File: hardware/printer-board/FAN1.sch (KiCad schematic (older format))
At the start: 8 parts, among them J39 TO FAN1, Q1 D882

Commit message: update,
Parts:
- J39: footprint footprint-lib:s2b-ph-kl,fan_output -> footprint-lib:b2b-ph-kl,fan_pwm_out
- Q1: footprint Package_TO_SOT_SMD:SOT-89-3 -> footprint-lib:SOT-89-3,thermal_vias
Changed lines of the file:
@@
 $Descr A4 11693 8268
 encoding utf-8
-Sheet 1 29
+Sheet 23 29
 Title ""
 Date ""
@@
 AR Path="/5CC2401E/5CC242A1/5CC8A035" Ref="J?"  Part="1"
 AR Path="/5CC2401E/5CC24321/5CC8A035" Ref="J39"  Part="1"
-AR Path="/5CC8A035" Ref="J1"  Part="1"
-F 0 "J39" H 4300 2550 50  0000 C CNN
-F 1 "TO FAN1" H 4300 2650 50  0000 C CNN
-F 2 "footprint-lib:s2b-ph-kl,fan_output" H 4350 2900 50  0001 C CNN
+AR Path="/5CC8A035" Ref="J39"  Part="1"
+F 0 "J39" H 4350 3000 50  0000 C CNN
+F 1 "TO FAN1" H 4350 2700 50  0000 C CNN
+F 2 "footprint-lib:b2b-ph-kl,fan_pwm_out" H 4350 2900 50  0001 C CNN
 F 3 "~" H 4350 2900 50  0001 C CNN
 	1    4350 2900
@@
 AR Path="/5CC2401E/5CC242A1/5CC8A041" Ref="C?"  Part="1"
 AR Path="/5CC2401E/5CC24321/5CC8A041" Ref="C34"  Part="1"
-AR Path="/5CC8A041" Ref="C1"  Part="1"
+AR Path="/5CC8A041" Ref="C34"  Part="1"
 F 0 "C34" V 3075 4750 50  0000 C CNN
 F 1 "CP100uf,16V" V 2984 4750 50  0000 C CNN
@@
 F 0 "Q1" H 3350 3700 50  0000 L CNN
 F 1 "D882" H 3350 3650 50  0000 L CNN
-F 2 "Package_TO_SOT_SMD:SOT-89-3" H 3350 3750 50  0001 C CNN
+F 2 "footprint-lib:SOT-89-3,thermal_vias" H 3350 3750 50  0001 C CNN
 F 3 "" H 3150 3650 50  0001 C CNN
 	1    3150 3650

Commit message: update to re-annotation,
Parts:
- renumbered C34 to C37, D2 to D21, J39 to J34, Q1 to Q5, R45 to R60, R46 to R61, R47 to R62, R37 to R63
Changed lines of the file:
@@
 AR Path="/5CC19D48/5CC8A035" Ref="J?"  Part="1"
 AR Path="/5CC2401E/5CC242A1/5CC8A035" Ref="J?"  Part="1"
-AR Path="/5CC2401E/5CC24321/5CC8A035" Ref="J39"  Part="1"
-AR Path="/5CC8A035" Ref="J39"  Part="1"
-F 0 "J39" H 4350 3000 50  0000 C CNN
+AR Path="/5CC2401E/5CC24321/5CC8A035" Ref="J34"  Part="1"
+AR Path="/5CC8A035" Ref="J?"  Part="1"
+F 0 "J34" H 4350 3000 50  0000 C CNN
 F 1 "TO FAN1" H 4350 2700 50  0000 C CNN
 F 2 "footprint-lib:b2b-ph-kl,fan_pwm_out" H 4350 2900 50  0001 C CNN
@@
 AR Path="/5CC19D48/5CC24372" Ref="R?"  Part="1"
 AR Path="/5CC2401E/5CC242A1/5CC24372" Ref="R?"  Part="1"
-AR Path="/5CC2401E/5CC24321/5CC24372" Ref="R45"  Part="1"
-AR Path="/5CC24372" Ref="R3"  Part="1"
-F 0 "R45" V 2304 3650 50  0000 C CNN
+AR Path="/5CC2401E/5CC24321/5CC24372" Ref="R60"  Part="1"
+AR Path="/5CC24372" Ref="R?"  Part="1"
+F 0 "R60" V 2304 3650 50  0000 C CNN
 F 1 "R100,0805" V 2395 3650 50  0000 C CNN
 F 2 "Resistor_SMD:R_0805_2012Metric_Pad1.15x1.40mm_HandSolder" H 2500 3650 50  0001 C CNN
@@
 AR Path="/5CC19D48/5CC8A032" Ref="R?"  Part="1"
 AR Path="/5CC2401E/5CC242A1/5CC8A032" Ref="R?"  Part="1"
-AR Path="/5CC2401E/5CC24321/5CC8A032" Ref="R46"  Part="1"
-AR Path="/5CC8A032" Ref="R4"  Part="1"
-F 0 "R46" V 2304 4050 50  0000 C CNN
+AR Path="/5CC2401E/5CC24321/5CC8A032" Ref="R61"  Part="1"
+AR Path="/5CC8A032" Ref="R?"  Part="1"
+F 0 "R61" V 2304 4050 50  0000 C CNN
 F 1 "R104,0805" V 2395 4050 50  0000 C CNN
 F 2 "Resistor_SMD:R_0805_2012Metric_Pad1.15x1.40mm_HandSolder" H 2500 4050 50  0001 C CNN
@@
 AR Path="/5CC19D48/5CC8A038" Ref="#PWR?"  Part="1"
 AR Path="/5CC2401E/5CC242A1/5CC8A038" Ref="#PWR?"  Part="1"
-AR Path="/5CC2401E/5CC24321/5CC8A038" Ref="#PWR0147"  Part="1"
-AR Path="/5CC8A038" Ref="#PWR0101"  Part="1"
-F 0 "#PWR0147" H 3250 4000 50  0001 C CNN
+AR Path="/5CC2401E/5CC24321/5CC8A038" Ref="#PWR0166"  Part="1"
+AR Path="/5CC8A038" Ref="#PWR?"  Part="1"
+F 0 "#PWR0166" H 3250 4000 50  0001 C CNN
 F 1 "GND" H 3255 4077 50  0000 C CNN
 F 2 "" H 3250 4250 50  0001 C CNN
@@
 AR Path="/5CC19D48/5CC242FD" Ref="R?"  Part="1"
 AR Path="/5CC2401E/5CC242A1/5CC242FD" Ref="R?"  Part="1"
-AR Path="/5CC2401E/5CC24321/5CC242FD" Ref="R37"  Part="1"
-AR Path="/5CC242FD" Ref="R1"  Part="1"
-F 0 "R37" H 3809 2546 50  0000 L CNN
+AR Path="/5CC2401E/5CC24321/5CC242FD" Ref="R63"  Part="1"
+AR Path="/5CC242FD" Ref="R?"  Part="1"
+F 0 "R63" H 3809 2546 50  0000 L CNN
 F 1 "R182,0603" H 3809 2455 50  0000 L CNN
 F 2 "Resistor_SMD:R_0603_1608Metric_Pad1.05x0.95mm_HandSolder" H 3750 2500 50  0001 C CNN
@@
 AR Path="/5CC19D48/5CC8A03B" Ref="#PWR?"  Part="1"
 AR Path="/5CC2401E/5CC242A1/5CC8A03B" Ref="#PWR?"  Part="1"
-AR Path="/5CC2401E/5CC24321/5CC8A03B" Ref="#PWR0152"  Part="1"
-AR Path="/5CC8A03B" Ref="#PWR0102"  Part="1"
-F 0 "#PWR0152" H 4000 2050 50  0001 C CNN
+AR Path="/5CC2401E/5CC24321/5CC8A03B" Ref="#PWR0167"  Part="1"
+AR Path="/5CC8A03B" Ref="#PWR?"  Part="1"
+F 0 "#PWR0167" H 4000 2050 50  0001 C CNN
 F 1 "+12V" H 4015 2373 50  0000 C CNN
 F 2 "" H 4000 2200 50  0001 C CNN
@@
 AR Path="/5CC19D48/5CC8A045" Ref="D?"  Part="1"
 AR Path="/5CC2401E/5CC242A1/5CC8A045" Ref="D?"  Part="1"
-AR Path="/5CC2401E/5CC24321/5CC8A045" Ref="D2"  Part="1"
-AR Path="/5CC8A045" Ref="D1"  Part="1"
-F 0 "D2" V 3704 2898 50  0000 L CNN
+AR Path="/5CC2401E/5CC24321/5CC8A045" Ref="D21"  Part="1"
+AR Path="/5CC8A045" Ref="D?"  Part="1"
+F 0 "D21" V 3704 2898 50  0000 L CNN
 F 1 "LED_BLUE,0603" V 3795 2898 50  0000 L CNN
 F 2 "LED_SMD:LED_0603_1608Metric_Pad1.05x0.95mm_HandSolder" V 3750 2800 50  0001 C CNN
@@
 AR Path="/5CC19D48/5CC8A03D" Ref="#PWR?"  Part="1"
 AR Path="/5CC2401E/5CC242A1/5CC8A03D" Ref="#PWR?"  Part="1"
-AR Path="/5CC2401E/5CC24321/5CC8A03D" Ref="#PWR0153"  Part="1"
-AR Path="/5CC8A03D" Ref="#PWR0103"  Part="1"
-F 0 "#PWR0153" H 2600 4600 50  0001 C CNN
+AR Path="/5CC2401E/5CC24321/5CC8A03D" Ref="#PWR0164"  Part="1"
+AR Path="/5CC8A03D" Ref="#PWR?"  Part="1"
+F 0 "#PWR0164" H 2600 4600 50  0001 C CNN
 F 1 "+12V" V 2615 4878 50  0000 L CNN
 F 2 "" H 2600 4750 50  0001 C CNN
@@
 AR Path="/5CC19D48/5CC8A03F" Ref="#PWR?"  Part="1"
 AR Path="/5CC2401E/5CC242A1/5CC8A03F" Ref="#PWR?"  Part="1"
-AR Path="/5CC2401E/5CC24321/5CC8A03F" Ref="#PWR0154"  Part="1"
-AR Path="/5CC8A03F" Ref="#PWR0104"  Part="1"
-F 0 "#PWR0154" H 3100 4500 50  0001 C CNN
+AR Path="/5CC2401E/5CC24321/5CC8A03F" Ref="#PWR0165"  Part="1"
+AR Path="/5CC8A03F" Ref="#PWR?"  Part="1"
+F 0 "#PWR0165" H 3100 4500 50  0001 C CNN
 F 1 "GND" H 3105 4577 50  0000 C CNN
 F 2 "" H 3100 4750 50  0001 C CNN
@@
 AR Path="/5CC19D48/5CC8A041" Ref="C?"  Part="1"
 AR Path="/5CC2401E/5CC242A1/5CC8A041" Ref="C?"  Part="1"
-AR Path="/5CC2401E/5CC24321/5CC8A041" Ref="C34"  Part="1"
-AR Path="/5CC8A041" Ref="C34"  Part="1"
-F 0 "C34" V 3075 4750 50  0000 C CNN
+AR Path="/5CC2401E/5CC24321/5CC8A041" Ref="C37"  Part="1"
+AR Path="/5CC8A041" Ref="C?"  Part="1"
+F 0 "C37" V 3075 4750 50  0000 C CNN
 F 1 "CP100uf,16V" V 2984 4750 50  0000 C CNN
 F 2 "Capacitor_SMD:CP_Elec_6.3x5.3" H 2850 4750 50  0001 C CNN
@@
 $EndBitmap
 $Comp
-L taobao-components:D882 Q1
+L taobao-components:D882 Q5
 U 1 1 5CC8A047
 P 3150 3650
-F 0 "Q1" H 3350 3700 50  0000 L CNN
+F 0 "Q5" H 3350 3700 50  0000 L CNN
 F 1 "D882" H 3350 3650 50  0000 L CNN
 F 2 "footprint-lib:SOT-89-3,thermal_vias" H 3350 3750 50  0001 C CNN
@@
 $EndComp
 $Comp
-L taobao-r:R100,0603 R47
+L taobao-r:R100,0603 R62
 U 1 1 5CC8A049
 P 3250 3150
-F 0 "R47" H 3350 3200 50  0000 L CNN
+F 0 "R62" H 3350 3200 50  0000 L CNN
 F 1 "R100,0603" H 3350 3150 50  0000 L CNN
 F 2 "Resistor_SMD:R_0603_1608Metric_Pad1.05x0.95mm_HandSolder" H 3250 3150 50  0001 C CNN

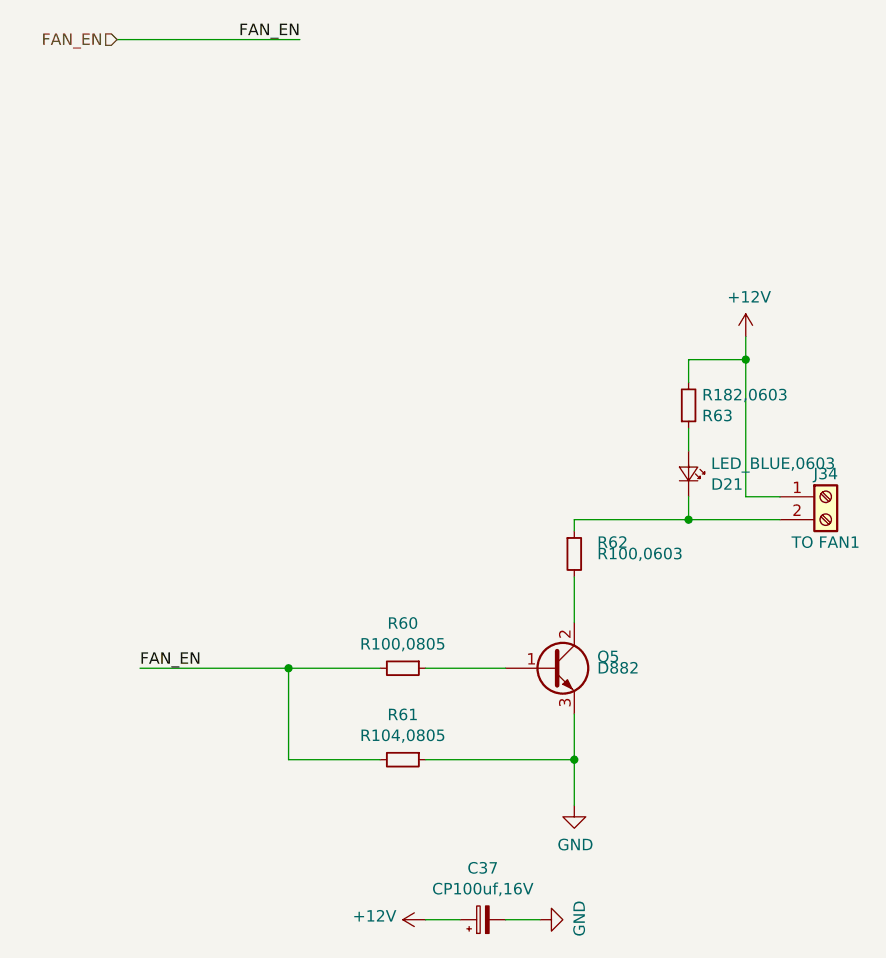
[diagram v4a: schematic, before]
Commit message: update step motor terminal orientation,
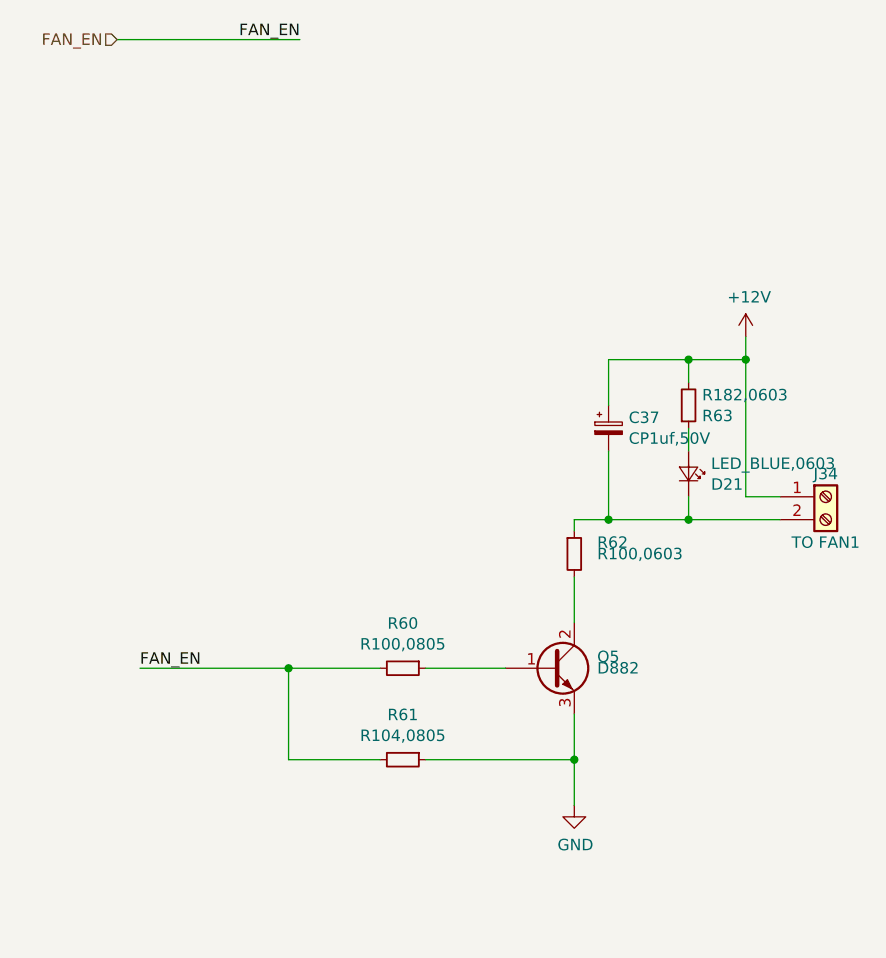
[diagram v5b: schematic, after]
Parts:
- removed C37: CP100uf,16V, Capacitor_SMD:CP_Elec_6.3x5.3, symbol taobao-cp:CP100uf,16V
- added C37: CP1uf,50V, Capacitor_SMD:CP_Elec_4x5.3, symbol taobao-cp:CP1uf,50V
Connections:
- net +12V: now also C37.1
- net at D21.1 (K), J34.2 (Pin_2), R62.1: now also C37.2
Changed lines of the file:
@@
 $Descr A4 11693 8268
 encoding utf-8
-Sheet 1 29
+Sheet 23 29
 Title ""
 Date ""
@@
 	0    1    -1   0
 $EndComp
-$Comp
-L power:+12V #PWR?
-U 1 1 5CC8A03D
-P 2600 4750
-AR Path="/5CC12903/5CC8A03D" Ref="#PWR?"  Part="1"
-AR Path="/5CC130A8/5CC8A03D" Ref="#PWR?"  Part="1"
-AR Path="/5CC19D48/5CC8A03D" Ref="#PWR?"  Part="1"
-AR Path="/5CC2401E/5CC242A1/5CC8A03D" Ref="#PWR?"  Part="1"
-AR Path="/5CC2401E/5CC24321/5CC8A03D" Ref="#PWR0164"  Part="1"
-AR Path="/5CC8A03D" Ref="#PWR0164"  Part="1"
-F 0 "#PWR0164" H 2600 4600 50  0001 C CNN
-F 1 "+12V" V 2615 4878 50  0000 L CNN
-F 2 "" H 2600 4750 50  0001 C CNN
-F 3 "" H 2600 4750 50  0001 C CNN
-	1    2600 4750
-	0    -1   -1   0
-$EndComp
-$Comp
-L power:GND #PWR?
-U 1 1 5CC8A03F
-P 3100 4750
-AR Path="/5CC0B758/5CC8A03F" Ref="#PWR?"  Part="1"
-AR Path="/5CC12903/5CC8A03F" Ref="#PWR?"  Part="1"
-AR Path="/5CC130A8/5CC8A03F" Ref="#PWR?"  Part="1"
-AR Path="/5CC19D48/5CC8A03F" Ref="#PWR?"  Part="1"
-AR Path="/5CC2401E/5CC242A1/5CC8A03F" Ref="#PWR?"  Part="1"
-AR Path="/5CC2401E/5CC24321/5CC8A03F" Ref="#PWR0165"  Part="1"
-AR Path="/5CC8A03F" Ref="#PWR0165"  Part="1"
-F 0 "#PWR0165" H 3100 4500 50  0001 C CNN
-F 1 "GND" H 3105 4577 50  0000 C CNN
-F 2 "" H 3100 4750 50  0001 C CNN
-F 3 "" H 3100 4750 50  0001 C CNN
-	1    3100 4750
-	0    -1   -1   0
-$EndComp
-$Comp
-L taobao-cp:CP100uf,16V C?
-U 1 1 5CC8A041
-P 2850 4750
-AR Path="/5CC12903/5CC8A041" Ref="C?"  Part="1"
-AR Path="/5CC19D48/5CC8A041" Ref="C?"  Part="1"
-AR Path="/5CC2401E/5CC242A1/5CC8A041" Ref="C?"  Part="1"
-AR Path="/5CC2401E/5CC24321/5CC8A041" Ref="C37"  Part="1"
-AR Path="/5CC8A041" Ref="C37"  Part="1"
-F 0 "C37" V 3075 4750 50  0000 C CNN
-F 1 "CP100uf,16V" V 2984 4750 50  0000 C CNN
-F 2 "Capacitor_SMD:CP_Elec_6.3x5.3" H 2850 4750 50  0001 C CNN
-F 3 "~" H 2850 4750 50  0001 C CNN
-	1    2850 4750
-	0    -1   -1   0
-$EndComp
-Wire Wire Line
-	2600 4750 2750 4750
-Wire Wire Line
-	2950 4750 3100 4750
 $Bitmap
 Pos 9550 5050
@@
 	4000 2200 4000 2300
 Wire Wire Line
-	3250 3000 3750 3000
+	3250 3000 3400 3000
 Wire Wire Line
 	3250 3000 3250 3050
@@
 	4000 2300 4000 2900
 Connection ~ 4000 2300
+$Comp
+L taobao-cp:CP1uf,50V C37
+U 1 1 5CCC3211
+P 3400 2600
+F 0 "C37" H 3488 2646 50  0000 L CNN
+F 1 "CP1uf,50V" H 3488 2555 50  0000 L CNN
+F 2 "Capacitor_SMD:CP_Elec_4x5.3" H 3400 2600 50  0001 C CNN
+F 3 "~" H 3400 2600 50  0001 C CNN
+	1    3400 2600
+	1    0    0    -1
+$EndComp
+Wire Wire Line
+	3750 2300 3400 2300
+Wire Wire Line
+	3400 2300 3400 2500
+Connection ~ 3750 2300
+Wire Wire Line
+	3400 2700 3400 3000
+Connection ~ 3400 3000
+Wire Wire Line
+	3400 3000 3750 3000
 $EndSCHEMATC

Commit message: update ROUTING,
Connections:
- net FAN_EN renamed FAN1_EN
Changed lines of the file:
@@
 $Descr A4 11693 8268
 encoding utf-8
-Sheet 23 27
+Sheet 21 28
 Title ""
 Date ""
@@
 AR Path="/5CC2401E/5CC24321/5CC8A035" Ref="J34"  Part="1"
 AR Path="/5CC8A035" Ref="J34"  Part="1"
-F 0 "J34" H 4350 3000 50  0000 C CNN
+AR Path="/5CC2401E/5CE3779A/5CC8A035" Ref="J?"  Part="1"
+F 0 "J?" H 4350 3000 50  0000 C CNN
 F 1 "TO FAN1" H 4350 2700 50  0000 C CNN
 F 2 "footprint-lib:b2b-ph-kl,fan_pwm_out" H 4350 2900 50  0001 C CNN
@@
 AR Path="/5CC2401E/5CC24321/5CC24372" Ref="R60"  Part="1"
 AR Path="/5CC24372" Ref="R60"  Part="1"
-F 0 "R60" V 2304 3650 50  0000 C CNN
+AR Path="/5CC2401E/5CE3779A/5CC24372" Ref="R?"  Part="1"
+F 0 "R?" V 2304 3650 50  0000 C CNN
 F 1 "R100,0805" V 2395 3650 50  0000 C CNN
 F 2 "Resistor_SMD:R_0805_2012Metric_Pad1.15x1.40mm_HandSolder" H 2500 3650 50  0001 C CNN
@@
 AR Path="/5CC2401E/5CC24321/5CC8A032" Ref="R61"  Part="1"
 AR Path="/5CC8A032" Ref="R61"  Part="1"
-F 0 "R61" V 2304 4050 50  0000 C CNN
+AR Path="/5CC2401E/5CE3779A/5CC8A032" Ref="R?"  Part="1"
+F 0 "R?" V 2304 4050 50  0000 C CNN
 F 1 "R104,0805" V 2395 4050 50  0000 C CNN
 F 2 "Resistor_SMD:R_0805_2012Metric_Pad1.15x1.40mm_HandSolder" H 2500 4050 50  0001 C CNN
@@
 AR Path="/5CC2401E/5CC24321/5CC8A038" Ref="#PWR0166"  Part="1"
 AR Path="/5CC8A038" Ref="#PWR0166"  Part="1"
-F 0 "#PWR0166" H 3250 4000 50  0001 C CNN
+AR Path="/5CC2401E/5CE3779A/5CC8A038" Ref="#PWR?"  Part="1"
+F 0 "#PWR?" H 3250 4000 50  0001 C CNN
 F 1 "GND" H 3255 4077 50  0000 C CNN
 F 2 "" H 3250 4250 50  0001 C CNN
@@
 AR Path="/5CC2401E/5CC24321/5CC242FD" Ref="R63"  Part="1"
 AR Path="/5CC242FD" Ref="R63"  Part="1"
-F 0 "R63" H 3809 2546 50  0000 L CNN
+AR Path="/5CC2401E/5CE3779A/5CC242FD" Ref="R?"  Part="1"
+F 0 "R?" H 3809 2546 50  0000 L CNN
 F 1 "R182,0603" H 3809 2455 50  0000 L CNN
 F 2 "Resistor_SMD:R_0603_1608Metric_Pad1.05x0.95mm_HandSolder" H 3750 2500 50  0001 C CNN
@@
 	4150 2900 4000 2900
 Text HLabel 1250 900  0    50   Input ~ 0
-FAN_EN
+FAN1_EN
 Text Label 2050 900  2    50   ~ 0
-FAN_EN
+FAN1_EN
 Wire Wire Line
 	1250 900  2050 900
 Text Label 1350 3650 0    50   ~ 0
-FAN_EN
+FAN1_EN
 Wire Wire Line
 	1350 3650 2000 3650
@@
 AR Path="/5CC2401E/5CC24321/5CC8A03B" Ref="#PWR0167"  Part="1"
 AR Path="/5CC8A03B" Ref="#PWR0167"  Part="1"
-F 0 "#PWR0167" H 4000 2050 50  0001 C CNN
+AR Path="/5CC2401E/5CE3779A/5CC8A03B" Ref="#PWR?"  Part="1"
+F 0 "#PWR?" H 4000 2050 50  0001 C CNN
 F 1 "+12V" H 4015 2373 50  0000 C CNN
 F 2 "" H 4000 2200 50  0001 C CNN
@@
 AR Path="/5CC2401E/5CC24321/5CC8A045" Ref="D21"  Part="1"
 AR Path="/5CC8A045" Ref="D21"  Part="1"
-F 0 "D21" V 3704 2898 50  0000 L CNN
+AR Path="/5CC2401E/5CE3779A/5CC8A045" Ref="D?"  Part="1"
+F 0 "D?" V 3704 2898 50  0000 L CNN
 F 1 "LED_BLUE,0603" V 3795 2898 50  0000 L CNN
 F 2 "LED_SMD:LED_0603_1608Metric_Pad1.05x0.95mm_HandSolder" V 3750 2800 50  0001 C CNN
@@
 U 1 1 5CC8A047
 P 3150 3650
-F 0 "Q5" H 3350 3700 50  0000 L CNN
+AR Path="/5CC2401E/5CC24321/5CC8A047" Ref="Q5"  Part="1"
+AR Path="/5CC2401E/5CE3779A/5CC8A047" Ref="Q?"  Part="1"
+F 0 "Q?" H 3350 3700 50  0000 L CNN
 F 1 "D882" H 3350 3650 50  0000 L CNN
 F 2 "footprint-lib:SOT-89-3,thermal_vias" H 3350 3750 50  0001 C CNN
@@
 U 1 1 5CC8A049
 P 3250 3150
-F 0 "R62" H 3350 3200 50  0000 L CNN
+AR Path="/5CC2401E/5CC24321/5CC8A049" Ref="R62"  Part="1"
+AR Path="/5CC2401E/5CE3779A/5CC8A049" Ref="R?"  Part="1"
+F 0 "R?" H 3350 3200 50  0000 L CNN
 F 1 "R100,0603" H 3350 3150 50  0000 L CNN
 F 2 "Resistor_SMD:R_0603_1608Metric_Pad1.05x0.95mm_HandSolder" H 3250 3150 50  0001 C CNN
@@
 U 1 1 5CCC3211
 P 3400 2600
-F 0 "C37" H 3488 2646 50  0000 L CNN
+AR Path="/5CC2401E/5CC24321/5CCC3211" Ref="C37"  Part="1"
+AR Path="/5CC2401E/5CE3779A/5CCC3211" Ref="C?"  Part="1"
+F 0 "C?" H 3488 2646 50  0000 L CNN
 F 1 "CP1uf,50V" H 3488 2555 50  0000 L CNN
 F 2 "Capacitor_SMD:CP_Elec_4x5.3" H 3400 2600 50  0001 C CNN
